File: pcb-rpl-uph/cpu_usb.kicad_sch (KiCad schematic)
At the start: 3 parts, among them U5 RPL_UPH_FCBGA1744

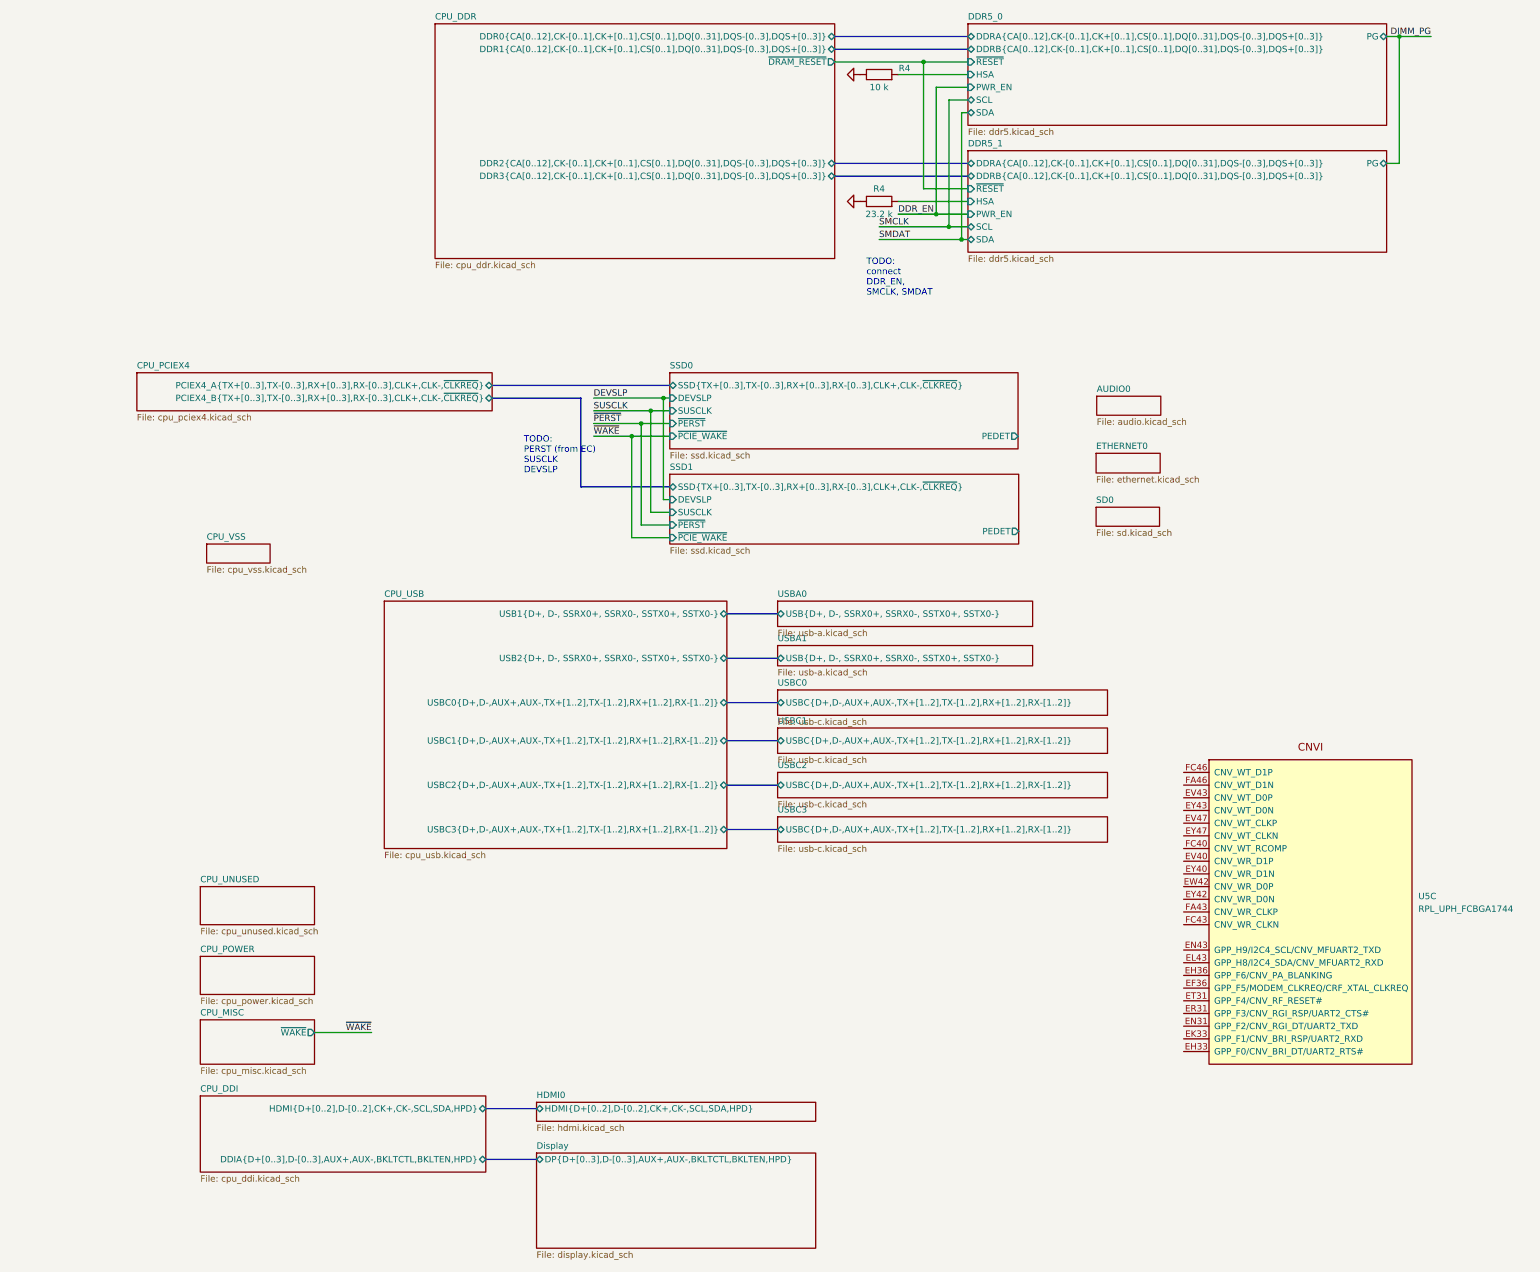
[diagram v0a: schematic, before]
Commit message: refactor much of CPU schematic symbol
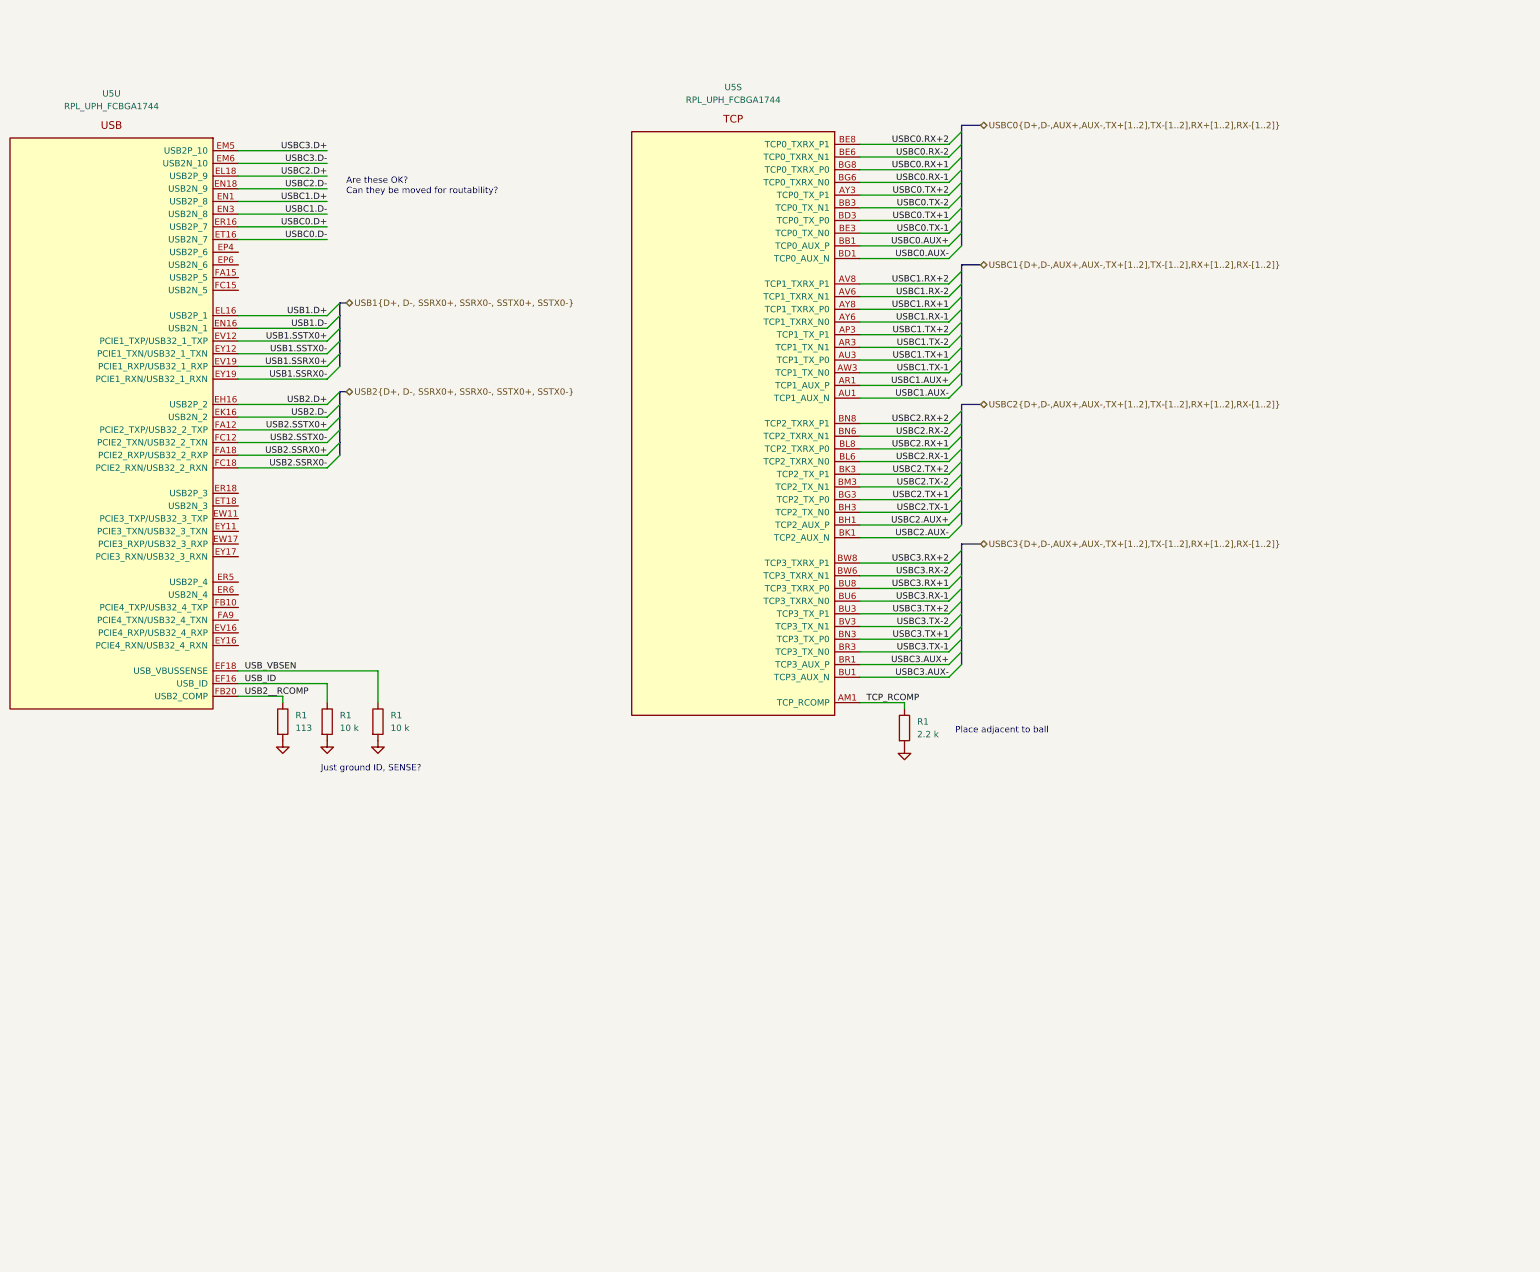
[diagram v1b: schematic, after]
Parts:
- removed R4: 23.2 k, local:R_0201_0603Metric, symbol Device:R
- removed R4: 10 k, local:R_0201_0603Metric, symbol Device:R
- removed U5: RPL_UPH_FCBGA1744, local:RPL_UPH_FCBGA1744, symbol local:RPL_UPH_FCBGA1744
- added R1: 2.2 k, local:R_0201_0603Metric, symbol Device:R
- added R1 (x2): 10 k, local:R_0201_0603Metric, symbol Device:R
- added R1: 113, local:R_0201_0603Metric, symbol Device:R
- added U5: RPL_UPH_FCBGA1744, local:RPL_UPH_FCBGA1744, symbol local:RPL_UPH_FCBGA1744
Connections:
- net GND: now also R1.2, R1.2, R1.2, R1.2
- new net TCP_RCOMP: R1.1, U5.AM1 (TCP_RCOMP)
- new net USB1.D+: U5.EL16 (USB2P_1)
- new net USB1.D-: U5.EN16 (USB2N_1)
- new net USB1.SSRX0+: U5.EV19 (PCIE1_RXP/USB32_1_RXP)
- new net USB1.SSRX0-: U5.EY19 (PCIE1_RXN/USB32_1_RXN)
- new net USB1.SSTX0+: U5.EV12 (PCIE1_TXP/USB32_1_TXP)
- new net USB1.SSTX0-: U5.EY12 (PCIE1_TXN/USB32_1_TXN)
- new net USB2.D+: U5.EH16 (USB2P_2)
- new net USB2.D-: U5.EK16 (USB2N_2)
- new net USB2.SSRX0+: U5.FA18 (PCIE2_RXP/USB32_2_RXP)
- new net USB2.SSRX0-: U5.FC18 (PCIE2_RXN/USB32_2_RXN)
- new net USB2.SSTX0+: U5.FA12 (PCIE2_TXP/USB32_2_TXP)
- new net USB2.SSTX0-: U5.FC12 (PCIE2_TXN/USB32_2_TXN)
- new net USB2__RCOMP: R1.1, U5.FB20 (USB2_COMP)
- new net USBC0.AUX+: U5.BB1 (TCP0_AUX_P)
- new net USBC0.AUX-: U5.BD1 (TCP0_AUX_N)
- new net USBC0.D+: U5.ER16 (USB2P_7)
- new net USBC0.D-: U5.ET16 (USB2N_7)
- new net USBC0.RX+1: U5.BG8 (TCP0_TXRX_P0)
- new net USBC0.RX+2: U5.BE8 (TCP0_TXRX_P1)
- new net USBC0.RX-1: U5.BG6 (TCP0_TXRX_N0)
- new net USBC0.RX-2: U5.BE6 (TCP0_TXRX_N1)
- new net USBC0.TX+1: U5.BD3 (TCP0_TX_P0)
- new net USBC0.TX+2: U5.AY3 (TCP0_TX_P1)
- new net USBC0.TX-1: U5.BE3 (TCP0_TX_N0)
- new net USBC0.TX-2: U5.BB3 (TCP0_TX_N1)
- new net USBC1.AUX+: U5.AR1 (TCP1_AUX_P)
- new net USBC1.AUX-: U5.AU1 (TCP1_AUX_N)
- new net USBC1.D+: U5.EN1 (USB2P_8)
- new net USBC1.D-: U5.EN3 (USB2N_8)
- new net USBC1.RX+1: U5.AY8 (TCP1_TXRX_P0)
- new net USBC1.RX+2: U5.AV8 (TCP1_TXRX_P1)
- new net USBC1.RX-1: U5.AY6 (TCP1_TXRX_N0)
- new net USBC1.RX-2: U5.AV6 (TCP1_TXRX_N1)
- new net USBC1.TX+1: U5.AU3 (TCP1_TX_P0)
- new net USBC1.TX+2: U5.AP3 (TCP1_TX_P1)
- new net USBC1.TX-1: U5.AW3 (TCP1_TX_N0)
- new net USBC1.TX-2: U5.AR3 (TCP1_TX_N1)
- new net USBC2.AUX+: U5.BH1 (TCP2_AUX_P)
- new net USBC2.AUX-: U5.BK1 (TCP2_AUX_N)
- new net USBC2.D+: U5.EL18 (USB2P_9)
- new net USBC2.D-: U5.EN18 (USB2N_9)
- new net USBC2.RX+1: U5.BL8 (TCP2_TXRX_P0)
- new net USBC2.RX+2: U5.BN8 (TCP2_TXRX_P1)
- new net USBC2.RX-1: U5.BL6 (TCP2_TXRX_N0)
- new net USBC2.RX-2: U5.BN6 (TCP2_TXRX_N1)
- new net USBC2.TX+1: U5.BG3 (TCP2_TX_P0)
- new net USBC2.TX+2: U5.BK3 (TCP2_TX_P1)
- new net USBC2.TX-1: U5.BH3 (TCP2_TX_N0)
- new net USBC2.TX-2: U5.BM3 (TCP2_TX_N1)
- new net USBC3.AUX+: U5.BR1 (TCP3_AUX_P)
- new net USBC3.AUX-: U5.BU1 (TCP3_AUX_N)
- new net USBC3.D+: U5.EM5 (USB2P_10)
- new net USBC3.D-: U5.EM6 (USB2N_10)
- new net USBC3.RX+1: U5.BU8 (TCP3_TXRX_P0)
- new net USBC3.RX+2: U5.BW8 (TCP3_TXRX_P1)
- new net USBC3.RX-1: U5.BU6 (TCP3_TXRX_N0)
- new net USBC3.RX-2: U5.BW6 (TCP3_TXRX_N1)
- new net USBC3.TX+1: U5.BN3 (TCP3_TX_P0)
- new net USBC3.TX+2: U5.BU3 (TCP3_TX_P1)
- new net USBC3.TX-1: U5.BR3 (TCP3_TX_N0)
- new net USBC3.TX-2: U5.BV3 (TCP3_TX_N1)
- new net USB_ID: R1.1, U5.EF16 (USB_ID)
- new net USB_VBSEN: R1.1, U5.EF18 (USB_VBUSSENSE)
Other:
- removed sheet AUDIO0
- removed sheet CPU_DDI
- removed sheet CPU_DDR
- removed sheet CPU_MISC
- removed sheet CPU_PCIEX4
- removed sheet CPU_POWER
- removed sheet CPU_UNUSED
- removed sheet CPU_USB
- removed sheet CPU_VSS
- removed sheet DDR5_0
- removed sheet DDR5_1
- removed sheet Display
- removed sheet ETHERNET0
- removed sheet HDMI0
- removed sheet SD0
- removed sheet SSD0
- removed sheet SSD1
- removed sheet USBA0
- removed sheet USBA1
- removed sheet USBC0
- removed sheet USBC1
- removed sheet USBC2
- removed sheet USBC3
- note added: "Are these OK? Can they be moved for routability?"
- note added: "Just ground ID, SENSE?"
- note added: "Place adjacent to ball"
- note removed: "TODO: PERST (from EC) SUSCLK DEVSLP"
- note removed: "TODO: connect DDR_EN, SMCLK, SMDAT"
